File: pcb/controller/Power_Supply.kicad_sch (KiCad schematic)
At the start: 80 parts, among them P2 USB_C_Plug_USB2.0, Q3 SI2301, SW8 SW_SPDT_312, U4 SIC438BED-T1-GE3, U5 TPS259474x, U6 TPS629206

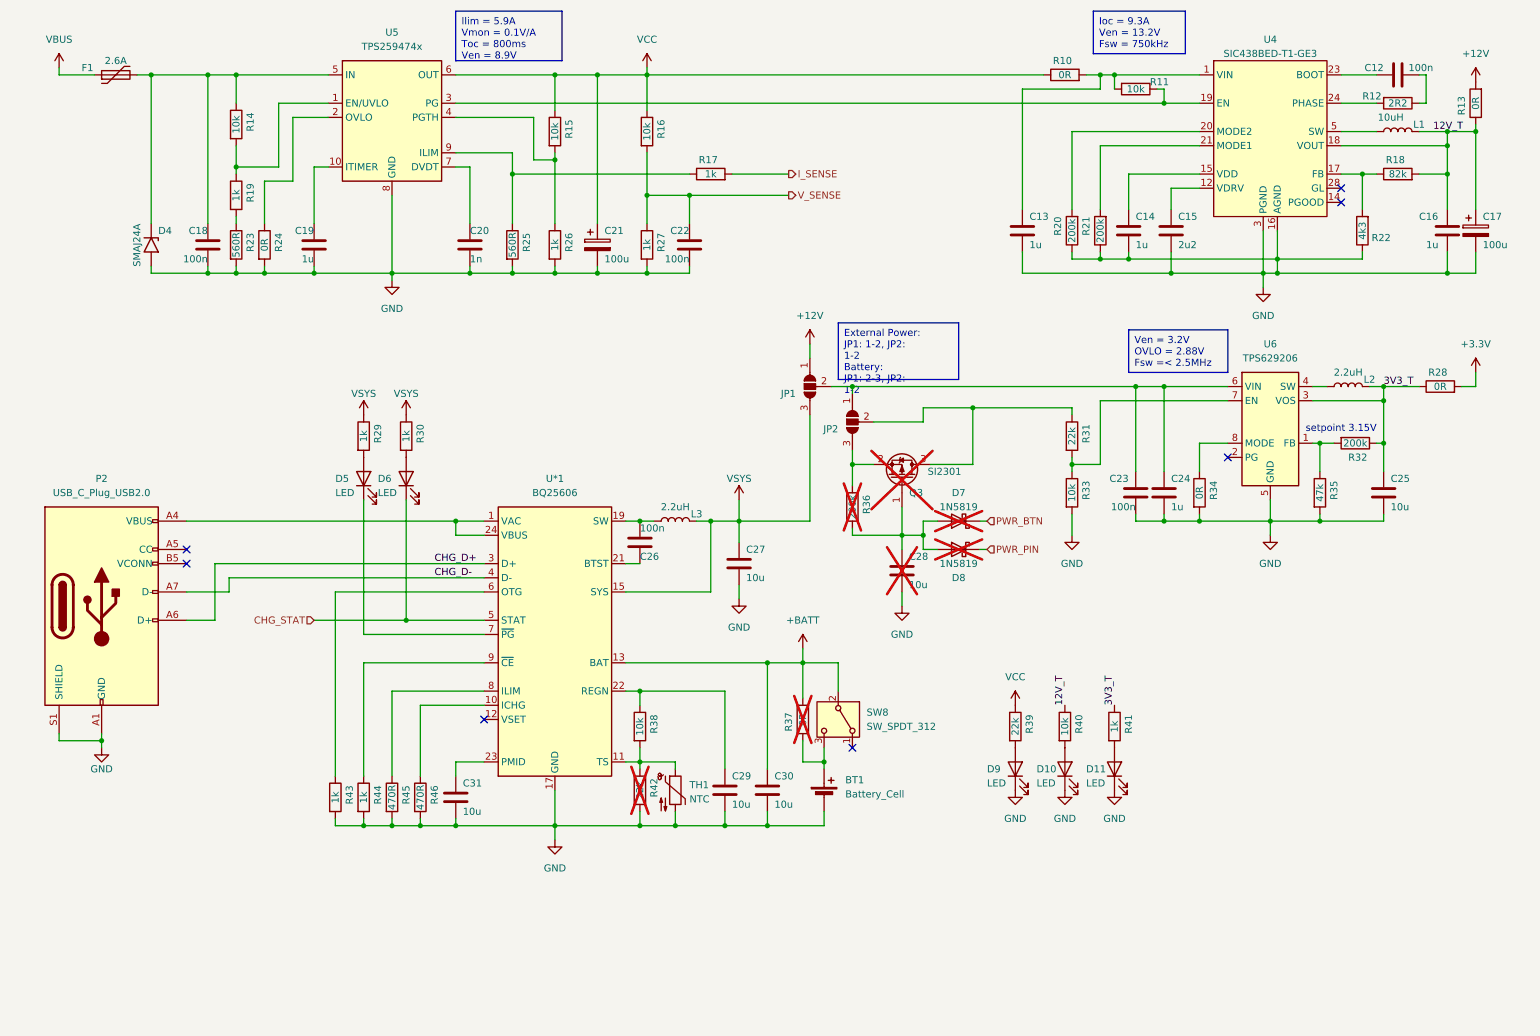
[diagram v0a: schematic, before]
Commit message: Revision 01 of Controller hardware
- fixed bugs from revision 00
- changed folder structure
- added ReleaseNotes_Controller.md to keep track of changes
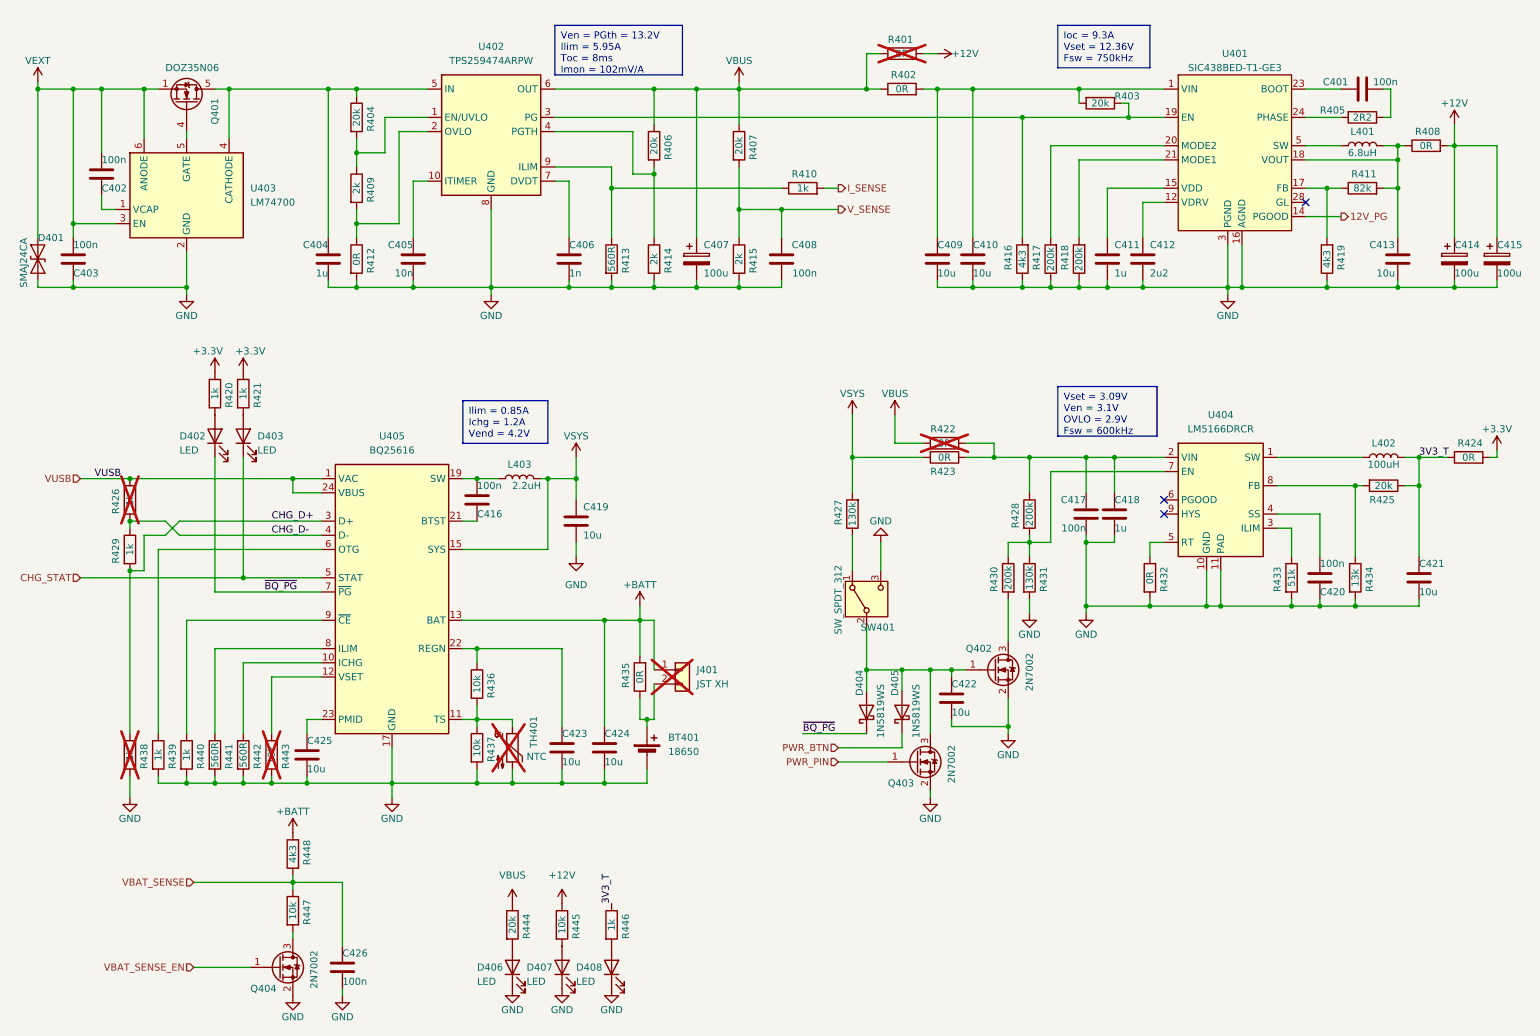
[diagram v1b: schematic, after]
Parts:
- removed C23: 100n, Capacitor_SMD:C_0402_1005Metric, symbol Device:C
- removed C24: 1u, Capacitor_SMD:C_0805_2012Metric, symbol Device:C
- removed C25, C28: 10u, Capacitor_SMD:C_0603_1608Metric, symbol Device:C
- removed D4: SMAJ24A, Diode_SMD:D_SMA, symbol Diode:SMAJ24A
- removed D7, D8: 1N5819, Diode_SMD:D_SOD-123, symbol Device:D_Schottky
- removed F1: 2.6A, Fuse:Fuse_2920_7451Metric, symbol Device:Polyfuse
- removed JP1, JP2: SolderJumper_3_Open, Jumper:SolderJumper-3_P1.3mm_Open_RoundedPad1.0x1.5mm_NumberLabels, symbol Jumper:SolderJumper_3_Open
- removed L2: 2.2uH, Inductor_SMD:L_1008_2520Metric, symbol Device:L
- removed P2: USB_C_Plug_USB2.0, Connector_USB:USB_C_Receptacle_G-Switch_GT-USB-7010ASV, symbol Connector:USB_C_Plug_USB2.0
- removed Q3: SI2301, Package_TO_SOT_SMD:SOT-23, symbol Device:Q_PMOS_GSD
- removed R24, R34: 0R, Resistor_SMD:R_0402_1005Metric, symbol Device:R
- removed R28: 0R, Resistor_SMD:R_0805_2012Metric, symbol Device:R
- removed R31: 22k, Resistor_SMD:R_0402_1005Metric, symbol Device:R
- removed R32, R36: 200k, Resistor_SMD:R_0402_1005Metric, symbol Device:R
- removed R33: 10k, Resistor_SMD:R_0402_1005Metric, symbol Device:R
- removed R35: 47k, Resistor_SMD:R_0402_1005Metric, symbol Device:R
- removed U6: TPS629206, Package_TO_SOT_SMD:SOT-583-8, symbol Ravenspark:TPS629206
- added C402, C403, C417, C420, C426: 100n, Capacitor_SMD:C_0402_1005Metric, symbol Device:C
- added C409: 10u, Capacitor_SMD:C_1206_3216Metric, symbol Device:C
- added C415: 100u, Capacitor_SMD:CP_Elec_8x10, symbol Device:C_Polarized
- added C418: 1u, Capacitor_SMD:C_0603_1608Metric, symbol Device:C
- added C421, C422: 10u, Capacitor_SMD:C_0603_1608Metric, symbol Device:C
- added D401: SMAJ24CA, Diode_SMD:D_SMA, symbol Diode:SMAJ24CA
- added D404, D405: 1N5819WS, Diode_SMD:D_SOD-323, symbol Diode:1N5819WS
- added J401: JST XH, Connector_JST:JST_XH_B2B-XH-A_1x02_P2.50mm_Vertical, symbol Connector_Generic:Conn_01x02
- added L402: 100uH, Inductor_SMD:L_Changjiang_FNR4030S, symbol Device:L
- added Q401: DOZ35N06, Package_SON:VSON-8_3.3x3.3mm_P0.65mm_NexFET, symbol Ravenspark:60N03D
- added Q402, Q403, Q404: 2N7002, Package_TO_SOT_SMD:SOT-23, symbol Transistor_FET:2N7002
- added R401: 0R, Resistor_SMD:R_1206_3216Metric, symbol Device:R
- added R416, R448: 4k3, Resistor_SMD:R_0402_1005Metric, symbol Device:R
- added R422, R423, R424: 0R, Resistor_SMD:R_0603_1608Metric, symbol Device:R
- added R425: 20k, Resistor_SMD:R_0402_1005Metric, symbol Device:R
- added R426, R429, R438: 1k, Resistor_SMD:R_0402_1005Metric, symbol Device:R
- added R427, R431: 130k, Resistor_SMD:R_0402_1005Metric, symbol Device:R
- added R428, R430: 200k, Resistor_SMD:R_0402_1005Metric, symbol Device:R
- added R432: 0R, Resistor_SMD:R_0402_1005Metric, symbol Device:R
- added R433: 51k, Resistor_SMD:R_0402_1005Metric, symbol Device:R
- added R434: 13k, Resistor_SMD:R_0402_1005Metric, symbol Device:R
- added R443, R447: 10k, Resistor_SMD:R_0402_1005Metric, symbol Device:R
- added U403: LM74700, Package_TO_SOT_SMD:SOT-23-6, symbol Power_Management:LM74700
- added U404: LM5166DRCR, Package_SON:Texas_S-PVSON-N10_ThermalVias, symbol Regulator_Switching:LM5166
- BT401: renamed from BT1; value Battery_Cell -> 18650; footprint Battery:BatteryHolder_Keystone_1042_1x18650 -> RVNSPRK_Electromechanical:BatteryHolder_SMD_1x18650; LCSC Part # (none) -> C2988620
- C401: renamed from C12; LCSC Part # (none) -> C307331
- C404: renamed from C18; value 100n -> 1u; footprint Capacitor_SMD:C_0402_1005Metric -> Capacitor_SMD:C_0603_1608Metric; LCSC Part # (none) -> C15849
- C405: renamed from C19; value 1u -> 10n; footprint Capacitor_SMD:C_0603_1608Metric -> Capacitor_SMD:C_0402_1005Metric; LCSC Part # (none) -> C15195
- C406: renamed from C20; LCSC Part # (none) -> C1523
- C407: renamed from C21; LCSC Part # (none) -> C5373402
- C408: renamed from C22; LCSC Part # (none) -> C307331
- C410: renamed from C13; value 1u -> 10u; footprint Capacitor_SMD:C_0805_2012Metric -> Capacitor_SMD:C_1206_3216Metric; LCSC Part # (none) -> C13585
- C411: renamed from C14; footprint Capacitor_SMD:C_0603_1608Metric -> Capacitor_SMD:C_0402_1005Metric; LCSC Part # (none) -> C52923
- C412: renamed from C15; LCSC Part # (none) -> C23630
- C413: renamed from C16; value 1u -> 10u; footprint Capacitor_SMD:C_0805_2012Metric -> Capacitor_SMD:C_1206_3216Metric; LCSC Part # (none) -> C13585
- C414: renamed from C17; LCSC Part # (none) -> C5373402
- C416: renamed from C26; LCSC Part # (none) -> C307331
- C419: renamed from C27; LCSC Part # (none) -> C19702
- C423: renamed from C29; LCSC Part # (none) -> C19702
- C424: renamed from C30; LCSC Part # (none) -> C19702
- C425: renamed from C31; LCSC Part # (none) -> C19702
- D402: renamed from D5; LCSC Part # (none) -> C2286
- D403: renamed from D6; LCSC Part # (none) -> C2286
- D406: renamed from D9; LCSC Part # (none) -> C2286
- D407: renamed from D10; LCSC Part # (none) -> C2286
- D408: renamed from D11; LCSC Part # (none) -> C2286
- L401: renamed from L1; value 10uH -> 6.8uH; LCSC Part # (none) -> C32712978
- L403: renamed from L3; LCSC Part # (none) -> C964122
- R402: renamed from R10; footprint Resistor_SMD:R_0805_2012Metric -> Resistor_SMD:R_1206_3216Metric
- R403: renamed from R11; value 10k -> 20k
- R404: renamed from R14; value 10k -> 20k
- R406: renamed from R15; value 10k -> 20k
- R407: renamed from R16; value 10k -> 20k
- R408: renamed from R13; footprint Resistor_SMD:R_0805_2012Metric -> Resistor_SMD:R_1206_3216Metric
- R409: renamed from R19; value 1k -> 2k
- R411: renamed from R18; footprint Resistor_SMD:R_0603_1608Metric -> Resistor_SMD:R_0402_1005Metric
- R412: renamed from R23; value 560R -> 0R
- R414: renamed from R26; value 1k -> 2k
- R415: renamed from R27; value 1k -> 2k
- R419: renamed from R22; footprint Resistor_SMD:R_0603_1608Metric -> Resistor_SMD:R_0402_1005Metric
- R435: renamed from R37; footprint Resistor_SMD:R_0805_2012Metric -> Resistor_SMD:R_0603_1608Metric; now fitted
- R437: renamed from R42; value 22k -> 10k; now fitted
- R441: renamed from R45; value 470R -> 560R
- R442: renamed from R46; value 470R -> 560R
- R444: renamed from R39; value 22k -> 20k
- SW401: renamed from SW8; LCSC Part # (none) -> C431548
- TH401: renamed from TH1; Field6 (none) -> C77131; LCSC Part # (none) -> C77131; now not fitted
- U401: renamed from U4; LCSC Part # (none) -> C511430
- U402: renamed from U5; value TPS259474x -> TPS259474ARPW; LCSC Part # (none) -> C3662807
- U405: renamed from U*1; value BQ25606 -> BQ25616; LCSC Part # (none) -> C2866447
- renumbered R12 to R405, R17 to R410, R25 to R413, R20 to R417, R21 to R418, R29 to R420, R30 to R421, R38 to R436, R43 to R439, R44 to R440, R40 to R445, R41 to R446
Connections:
- net VCC is gone; now on net VBUS: C407.1, R402.1, R406.1, R407.1, R444.1, U402.6 (OUT)
- net +12V: now also C414.1, R445.1, C415.1, R401.1
- net +3.3V: now also R420.1, R421.1, R424.2
- net +BATT: now also J401.1 (Pin_1), R448.2; no longer SW401.2 (B)
- net 3V3_T: now also C421.1, L402.2, R424.1, R425.1
- net AGND: now also SW401.3 (C), C403.2, C409.2, C415.2, C417.1, C418.2, C420.1, C421.2, C422.2, C426.1, D401.2 (A2), Q402.2 (S), Q403.2 (S), Q404.2 (S), R416.1, R431.2, R432.2, R433.2, R434.2, R438.2, R443.2, U403.2 (GND), U404.10 (GND), U404.11 (PAD)
- net CHG_D+: now also R429.2, R438.1
- net CHG_D-: now also R426.2, R429.1
- net PWR_BTN: now also D405.1 (K)
- net PWR_PIN: now also Q403.1 (G)
- net VBUS: now also R401.2, R422.2
- net VIN: now also C409.1
- net VSYS: now also R423.2, R427.2; no longer R420.1, R421.1
- net at U402.2 (OVLO): now also R409.2, R412.1
- net at BT401.1 (+), R435.1: now also J401.2 (Pin_2); no longer SW401.3 (C)
- net at R403.1, U401.19 (EN), U402.3 (PG): now also R416.2
- net at C404.2, R404.1, U402.5 (IN): now also Q401.5 (D), U403.4 (CATHODE)
- net ~{BQ_PG}: now reaches D402.1 (K), U405.7 (~{PG})
- net ~{BQ_PG}: now also D404.1 (K)
- net VUSB: now reaches U405.1 (VAC), U405.24 (VBUS)
- net VUSB: now also R426.1
- net at U405.12 (VSET): now also R443.1
- net 12V_PG: now reaches U401.14 (PGOOD)
- net at SW401.1 (A): now also R427.1
- net 12V_T: no longer names the net of C413.1, L401.2, R408.1, R411.2, U401.18 (VOUT)
- net 12V_T: no longer C414.1, R445.1
- new net: C422.1, D404.2 (A), D405.2 (A), Q402.1 (G), Q403.3 (D), SW401.2 (B)
- new net: Q402.3 (D), R430.2
- new net: C417.2, C418.1, R422.1, R423.1, R428.1, U404.2 (VIN)
- new net: C402.2, U403.1 (VCAP)
- new net: Q401.4 (G), U403.5 (GATE)
- new net: R433.1, U404.3 (ILIM)
- new net: Q404.3 (D), R447.2
- new net: R432.1, U404.5 (RT)
- new net: R428.2, R430.1, R431.1, U404.7 (EN)
- new net: R425.2, R434.1, U404.8 (FB)
- new net: L402.1, U404.1 (SW)
- new net: C420.2, U404.4 (SS)
- new net VBAT_SENSE: C426.2, R447.1, R448.1
- new net VBAT_SENSE_EN: Q404.1 (G)
- new net VEXT: C402.1, C403.1, D401.1 (A1), Q401.1 (S), Q401.2 (S), Q401.3 (S), U403.3 (EN), U403.6 (ANODE)
- no-connect marks 7 -> 3
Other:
- note removed: "setpoint 3.15V"
- moved on the sheet: BT401, C401, C404, C405, C406, C407, C408, C410, C411, C412, C413, C414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

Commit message: Final adjustments and BOM optimization
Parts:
- added R449, R450: 0R, Resistor_SMD:R_0402_1005Metric, symbol Device:R
- C403: value 100n -> 1u; footprint Capacitor_SMD:C_0402_1005Metric -> Capacitor_SMD:C_0603_1608Metric; LCSC Part # C307331 -> C15849
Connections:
- net +3.3V: now also R449.1
- net VBAT_SENSE_EN: now also R450.1; no longer Q404.1 (G)
- new net: Q404.1 (G), R449.2, R450.2
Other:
- moved on the sheet: C417, C418

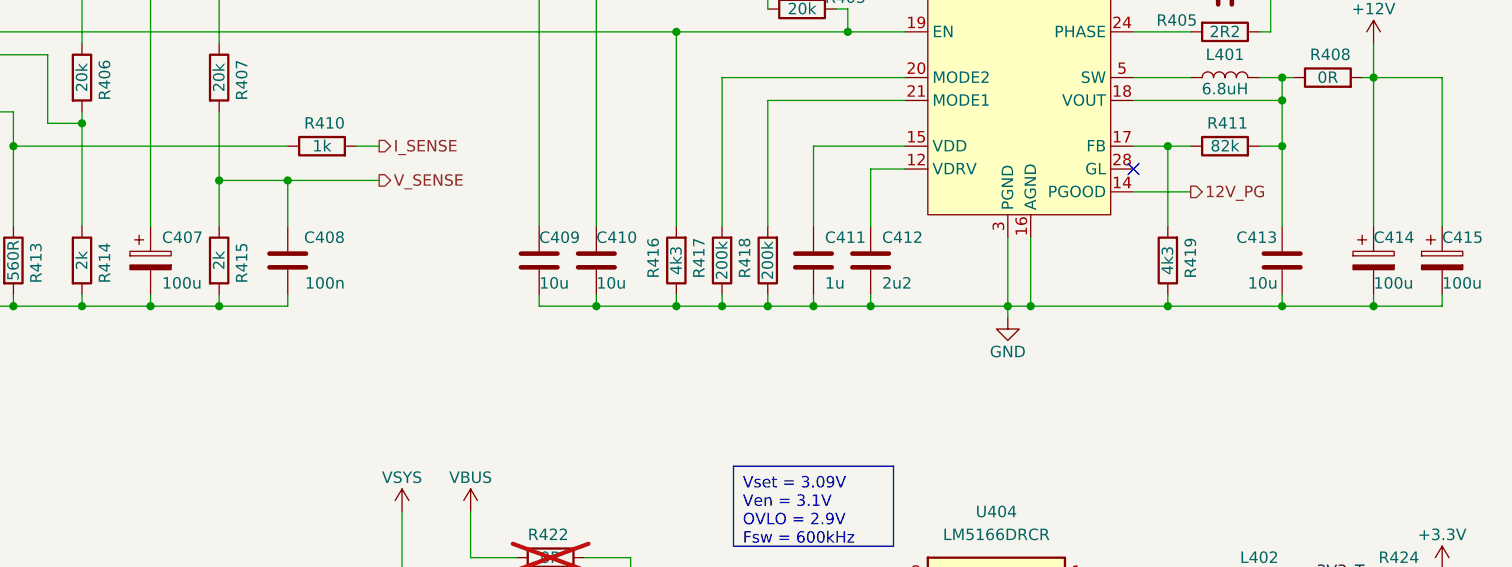
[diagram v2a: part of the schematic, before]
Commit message: Update wrong values after import in JLC for production
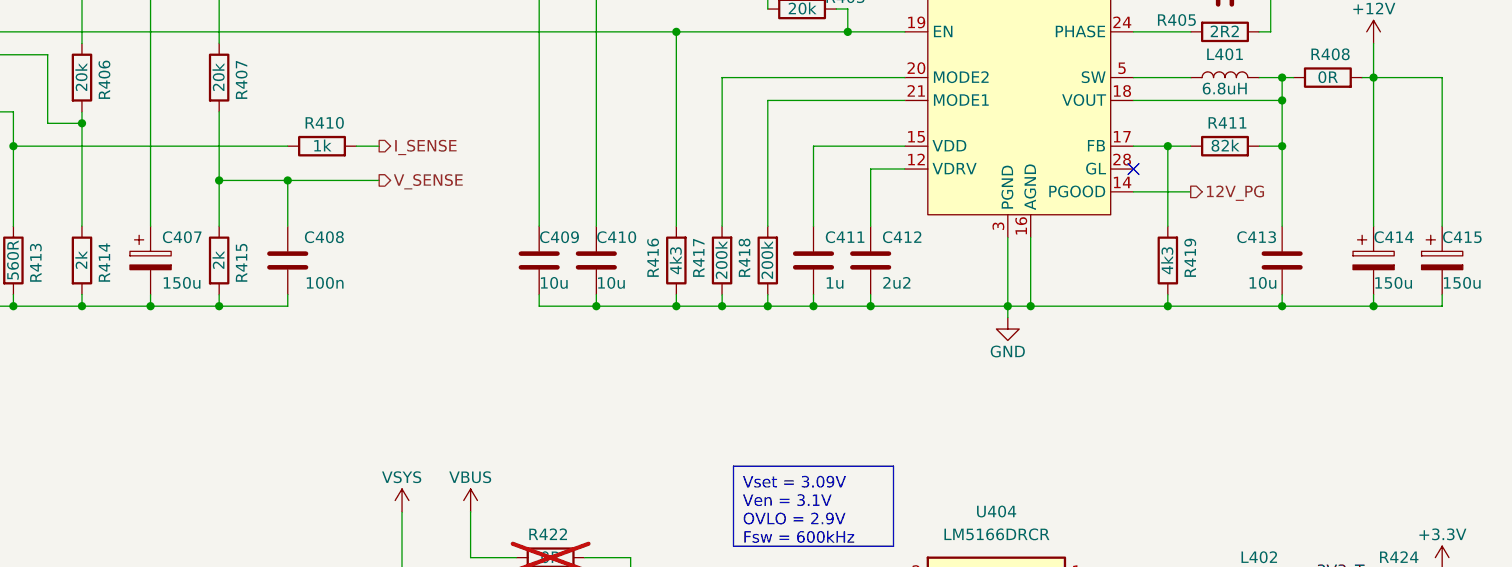
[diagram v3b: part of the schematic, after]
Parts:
- C407, C414, C415: value 100u -> 150u; LCSC Part # C5373402 -> C2898894
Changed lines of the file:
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@@
 	(title_block
 		(title "Power Supply")
-		(date "2025-04-09")
+		(date "2025-04-11")
 		(rev "01")
 		(company "Ravenspark")
@@
 			)
 		)
-		(property "Value" "100u"
+		(property "Value" "150u"
 			(at 279.4 60.96 0)
 			(effects
@@
 			)
 		)
-		(property "LCSC Part #" "C5373402"
+		(property "LCSC Part #" "C2898894"
 			(at 279.4 58.42 0)
 			(effects
@@
 			)
 		)
-		(property "Value" "100u"
+		(property "Value" "150u"
 			(at 271.78 60.96 0)
 			(effects
@@
 			)
 		)
-		(property "LCSC Part #" "C5373402"
+		(property "LCSC Part #" "C2898894"
 			(at 271.78 58.42 0)
 			(effects
@@
 			)
 		)
-		(property "Value" "100u"
+		(property "Value" "150u"
 			(at 137.16 60.96 0)
 			(effects
@@
 			)
 		)
-		(property "LCSC Part #" "C5373402"
+		(property "LCSC Part #" "C2898894"
 			(at 135.89 58.42 0)
 			(effects
